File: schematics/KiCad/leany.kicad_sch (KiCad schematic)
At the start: 25 parts, among them J1 SWD, J2 SSD1306, SW1 BOOTMODE_SW, SW2 ZERO_BTN, SW3 HOLD_BTN, U1 LSM6DSO, U2 STM32F103C8Tx, U3 CH340C, Y1 8MHz

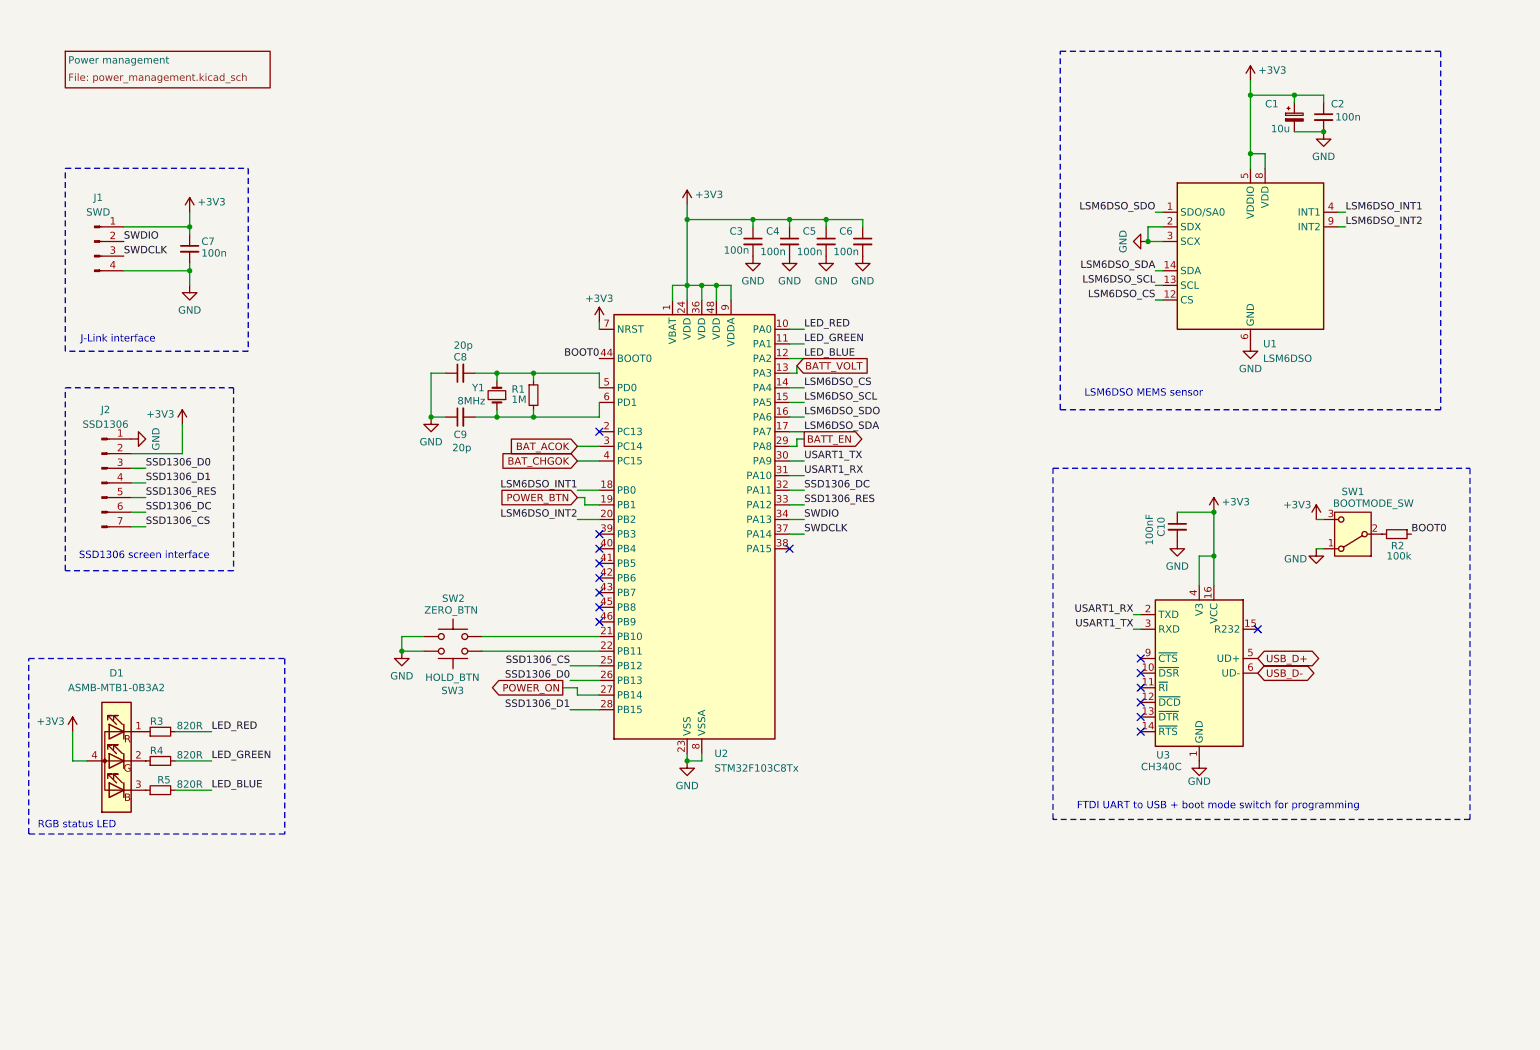
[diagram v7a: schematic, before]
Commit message: feat: Implement the ST7735S (#4)
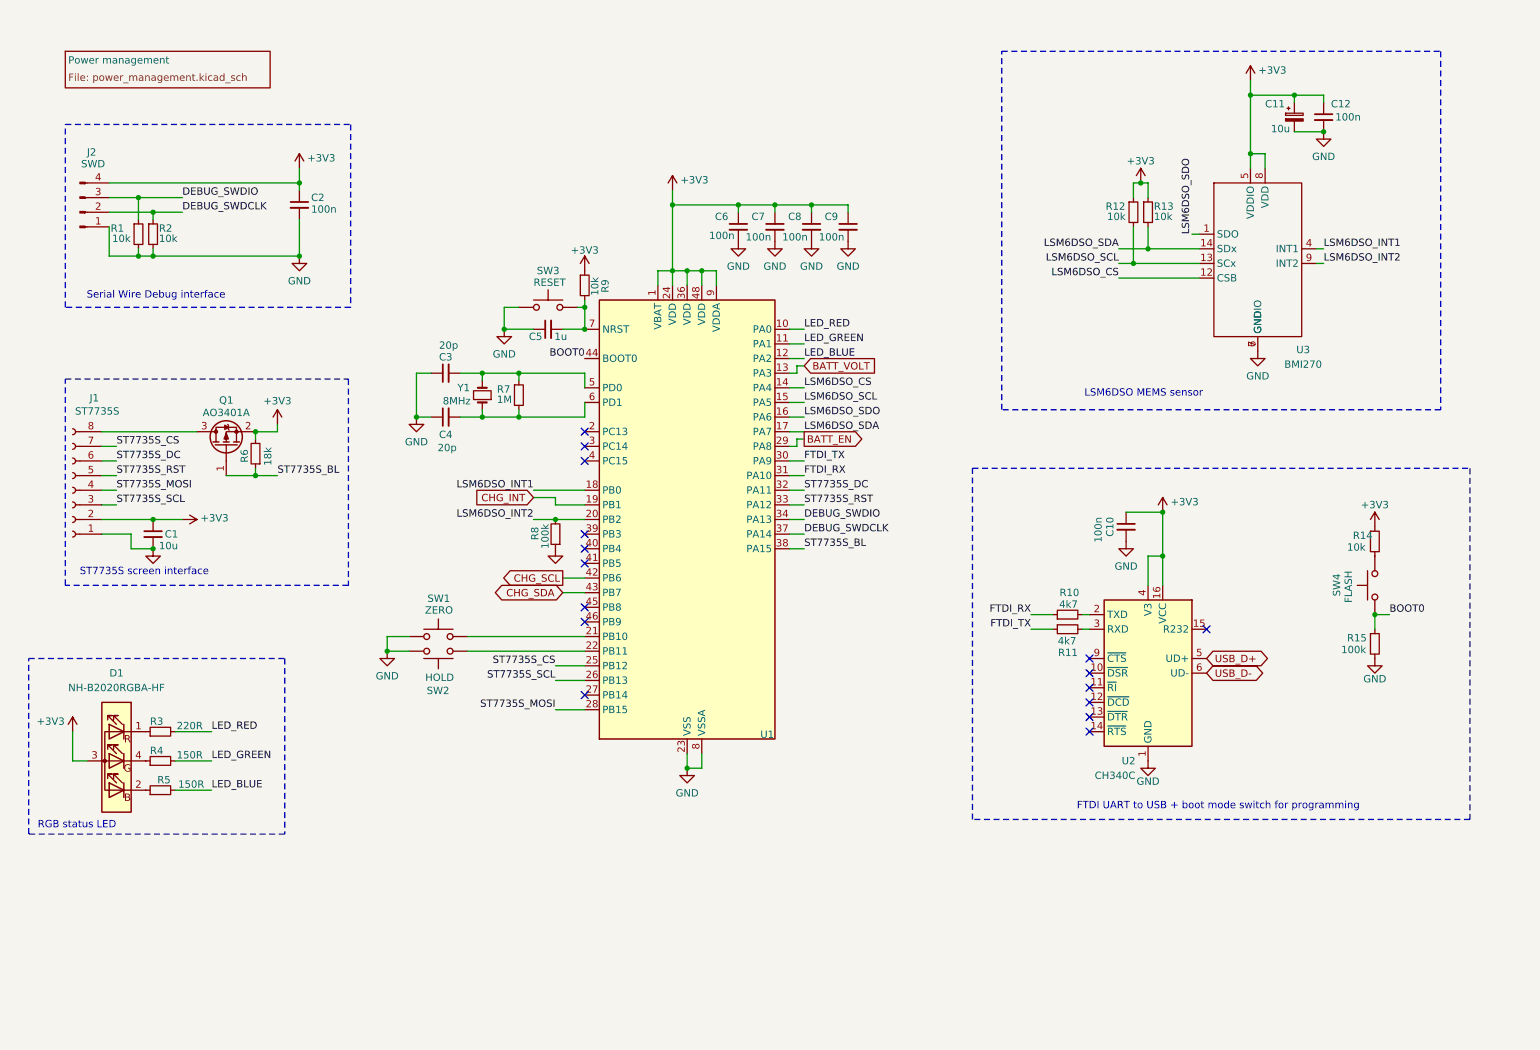
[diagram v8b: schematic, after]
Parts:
- removed D1: ASMB-MTB1-0B3A2, LED_SMD:LED_Avago_PLCC4_3.2x2.8mm_CW, symbol LED:ASMB-MTB1-0A3A2
- removed J2: SSD1306, Connector_PinHeader_1.00mm:PinHeader_1x07_P1.00mm_Vertical, symbol Connector:Conn_01x07_Pin
- removed SW1: BOOTMODE_SW, symbol Switch:SW_SPDT
- removed U1: LSM6DSO, Package_LGA:LGA-14_3x2.5mm_P0.5mm_LayoutBorder3x4y, symbol leany-symbols:LSM6DSO
- removed U3: CH340C, Package_SO:SOIC-16_3.9x9.9mm_P1.27mm, symbol Interface_USB:CH340C
- added C1: 10u, Capacitor_SMD:C_0805_2012Metric, symbol Device:C_Small
- added C5: 1u, Capacitor_SMD:C_0603_1608Metric, symbol Device:C_Small
- added D1: NH-B2020RGBA-HF, leany_footprints:NH-B2020RGBA-HF, symbol leany-symbols:NH-B2020RGBA-HF
- added J1: ST7735S, leany_footprints:ST7735S, symbol Connector:Conn_01x08_Socket
- added Q1: AO3401A, Package_TO_SOT_SMD:SOT-23, symbol Transistor_FET:AO3401A
- added R1, R12, R13, R14, R9: 10k, Resistor_SMD:R_0603_1608Metric, symbol Device:R_Small
- added R10, R11: 4k7, Resistor_SMD:R_0603_1608Metric, symbol Device:R_Small
- added R15, R8: 100k, Resistor_SMD:R_0603_1608Metric, symbol Device:R_Small
- added R6: 18k, Resistor_SMD:R_0603_1608Metric, symbol Device:R_Small
- added SW3: RESET, Button_Switch_SMD:SW_Push_1P1T_XKB_TS-1187A, symbol Switch:SW_Push
- added SW4: FLASH, Button_Switch_SMD:SW_Push_1P1T_XKB_TS-1187A, symbol Switch:SW_Push
- added U2: CH340C, Package_SO:SOIC-16_3.9x9.9mm_P1.27mm, symbol leany-symbols:CH340C
- added U3: BMI270, Package_LGA:LGA-14_3x2.5mm_P0.5mm_LayoutBorder3x4y, symbol leany-symbols:BMI270
- C10: value 100nF -> 100n; footprint Capacitor_SMD:C_0201_0603Metric -> Capacitor_SMD:C_0603_1608Metric; LCSC (none) -> C14663
- C11: renamed from C1; footprint (none) -> Capacitor_SMD:C_0805_2012Metric; LCSC (none) -> C15850
- C12: renamed from C2; footprint Capacitor_SMD:C_0201_0603Metric -> Capacitor_SMD:C_0603_1608Metric; LCSC (none) -> C14663
- C2: renamed from C7; footprint Capacitor_SMD:C_0201_0603Metric -> Capacitor_SMD:C_0603_1608Metric; LCSC (none) -> C14663
- C3: renamed from C8; footprint Capacitor_SMD:C_0201_0603Metric -> Capacitor_SMD:C_0603_1608Metric; LCSC (none) -> C1648
- C4: renamed from C9; footprint Capacitor_SMD:C_0201_0603Metric -> Capacitor_SMD:C_0603_1608Metric; LCSC (none) -> C1648
- C6: renamed from C3; footprint Capacitor_SMD:C_0201_0603Metric -> Capacitor_SMD:C_0603_1608Metric; LCSC (none) -> C14663
- C7: renamed from C4; footprint Capacitor_SMD:C_0201_0603Metric -> Capacitor_SMD:C_0603_1608Metric; LCSC (none) -> C14663
- C8: renamed from C5; footprint Capacitor_SMD:C_0201_0603Metric -> Capacitor_SMD:C_0603_1608Metric; LCSC (none) -> C14663
- C9: renamed from C6; footprint Capacitor_SMD:C_0201_0603Metric -> Capacitor_SMD:C_0603_1608Metric; LCSC (none) -> C14663
- J2: renamed from J1; footprint Connector_PinHeader_1.00mm:PinHeader_1x04_P1.00mm_Vertical -> Connector_PinHeader_2.54mm:PinHeader_1x04_P2.54mm_Horizontal; LCSC (none) -> C2935929
- R2: value 100k -> 10k; LCSC (none) -> C25804
- R3: value 820R -> 220R; LCSC (none) -> C22962
- R4, R5: value 820R -> 150R; LCSC (none) -> C22808
- R7: renamed from R1; LCSC (none) -> C22935
- SW1: renamed from SW2; value ZERO_BTN -> ZERO; footprint (none) -> leany_footprints:SW_Push_1P1T_NO_6x6mm_H9.5mm; LCSC (none) -> C455120
- SW2: renamed from SW3; value HOLD_BTN -> HOLD; footprint (none) -> leany_footprints:SW_Push_1P1T_NO_6x6mm_H9.5mm; LCSC (none) -> C455120
- U1: renamed from U2; LCSC (none) -> C8734
- Y1: footprint Crystal:Crystal_SMD_Abracon_ABM3-2Pin_5.0x3.2mm -> leany_footprints:Crystal_SMD_Abracon_ABM3-2Pin_5.0x3.2mm; LCSC (none) -> C115962
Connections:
- net +3V3: now also J2.4 (Pin_4), C1.1, D1.3 (A), J1.2 (Pin_2), Q1.2 (S), R12.1, R13.1, R14.1, R6.2, R9.1, U2.16 (VCC), U2.4 (V3), U3.5 (VDDIO), U3.8 (VDD); no longer J2.1 (Pin_1), U1.7 (NRST)
- net BOOT0: now also R15.1, SW4.2; no longer R2.1
- net GND: now also J2.1 (Pin_1), R2.2, C1.2, C5.1, J1.1 (Pin_1), R1.2, R15.2, R8.1, SW3.1, U2.1 (GND), U3.6 (GNDIO), U3.7 (GND); no longer J2.4 (Pin_4)
- net LSM6DSO_CS: now also U3.12 (CSB)
- net LSM6DSO_INT1: now also U3.4 (INT1)
- net LSM6DSO_INT2: now also R8.2, U3.9 (INT2)
- net LSM6DSO_SCL: now also R12.2, U3.13 (SCx)
- net LSM6DSO_SDA: now also R13.2, U3.14 (SDx)
- net LSM6DSO_SDO: now also U3.1 (SDO)
- net USB_D+: now also U2.5 (UD+)
- net USB_D-: now also U2.6 (UD-)
- net at R3.1: now also D1.1 (RK)
- net at R4.1: now also D1.4 (GK)
- net at R5.1: now also D1.2 (BK)
- net ST7735S_BL: now reaches U1.38 (PA15)
- net ST7735S_BL: now also Q1.1 (G), R6.1
- net CHG_SCL: now reaches U1.42 (PB6)
- net CHG_SDA: now reaches U1.43 (PB7)
- net BAT_ACOK: no longer names the net of U1.3 (PC14)
- net BAT_CHGOK: no longer names the net of U1.4 (PC15)
- net POWER_BTN renamed CHG_INT
- net POWER_ON: no longer names the net of U1.27 (PB14)
- net SSD1306_CS renamed ST7735S_CS
- net ST7735S_CS: now also J1.7 (Pin_7)
- net SSD1306_D0 renamed ST7735S_SCL
- net ST7735S_SCL: now also J1.3 (Pin_3)
- net SSD1306_D1 renamed ST7735S_MOSI
- net ST7735S_MOSI: now also J1.4 (Pin_4)
- net SSD1306_DC renamed ST7735S_DC
- net ST7735S_DC: now also J1.6 (Pin_6)
- net SSD1306_RES renamed ST7735S_RST
- net ST7735S_RST: now also J1.5 (Pin_5)
- net SWDCLK renamed DEBUG_SWDCLK
- net DEBUG_SWDCLK: now also J2.2 (Pin_2), R2.1; no longer J2.3 (Pin_3)
- net SWDIO renamed DEBUG_SWDIO
- net DEBUG_SWDIO: now also J2.3 (Pin_3), R1.1; no longer J2.2 (Pin_2)
- net USART1_RX renamed FTDI_RX
- net FTDI_RX: now also R10.1
- net USART1_TX renamed FTDI_TX
- net FTDI_TX: now also R11.1
- new net: R10.2, U2.2 (TXD)
- new net: R11.2, U2.3 (RXD)
- new net: C5.2, R9.2, SW3.2, U1.7 (NRST)
- new net: R14.2, SW4.1
- new net: J1.8 (Pin_8), Q1.3 (D)
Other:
- note added: "ST7735S screen interface"
- note added: "Serial Wire Debug interface"
- note removed: "J-Link interface"
- note removed: "SSD1306 screen interface"
- moved on the sheet: C10, C2, C3, C4, C6, C7, C8, C9, J2, R7, SW1, SW2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
